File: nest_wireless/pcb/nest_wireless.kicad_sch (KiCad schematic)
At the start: 74 parts, among them J3 Conn_01x04, J4 FFC2B35-12-G_REVA2, SW1 SW_PUSH, SW10 SW_PUSH, SW11 SW_PUSH, SW12 SW_PUSH, SW13 SW_PUSH, SW14 SW_PUSH, SW15 SW_PUSH, SW16 SW_PUSH, SW17 SW_PUSH, SW18 SW_PUSH, SW19 SW_PUSH, SW2 SW_PUSH, SW20 SW_PUSH, SW21 SW_PUSH, SW22 SW_PUSH, SW23 SW_PUSH, SW24 SW_PUSH, SW25 Rotary_Encoder_Switch-Device, SW26 SW_PUSH, SW27 SW_PUSH, SW28 SW_PUSH, SW29 SW_PUSH, SW3 SW_PUSH, SW30 SW_PUSH, SW4 SW_PUSH, SW5 SW_PUSH, SW6 SW_PUSH, SW7 SW_PUSH, SW8 SW_PUSH, SW9 SW_PUSH, U2 kb2040

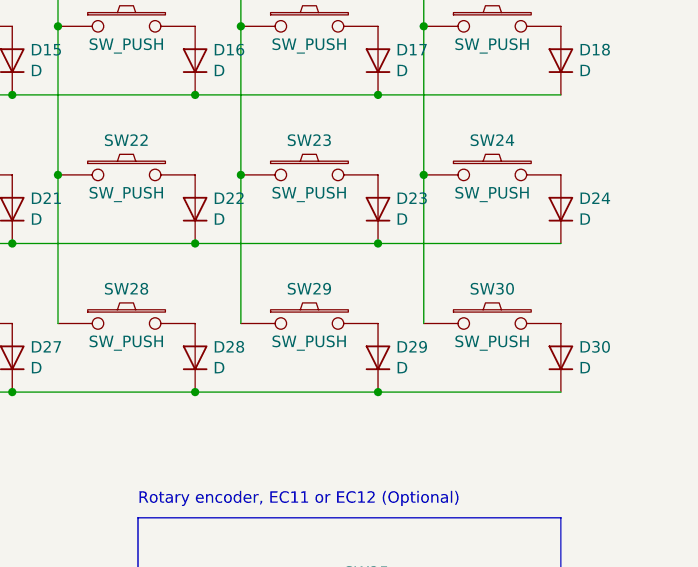
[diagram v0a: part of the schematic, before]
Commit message: Clean up a few design rule violations
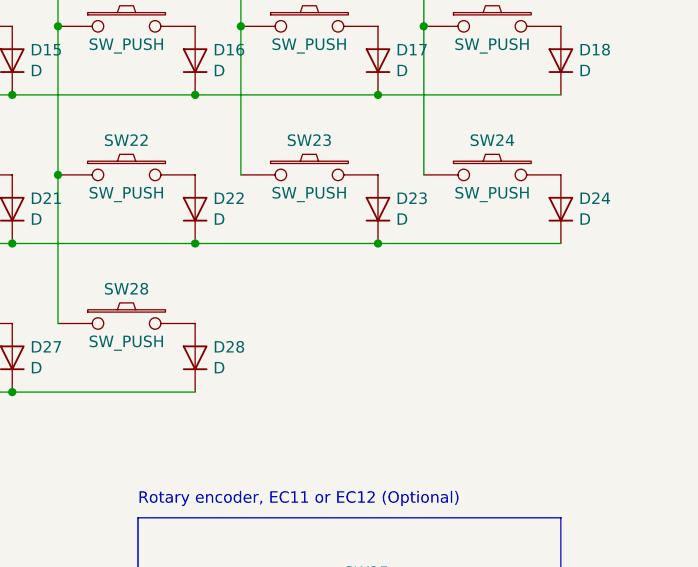
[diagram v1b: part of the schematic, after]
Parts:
- removed D29, D30: D, NestWireless:D_SOD-123_DO-35_Hybrid_DoubleSided_V2, symbol NestWireless:Key_Diode
- removed SW29, SW30: SW_PUSH, NestWireless:Cherry_MX_DS_Hotswap_v3.5.4, symbol NestWireless:SW_PUSH

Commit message: Nest wireless kicad project cleanup
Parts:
- added J1: Conn_01x05, symbol Connector_Generic:Conn_01x05
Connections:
- net ENCA: now also U2.2 (D0); no longer U2.9 (D5)
- net ENCB: now also U2.3 (D1); no longer U2.8 (D4)
- net GND: now also J1.2 (Pin_2)
- net VCC: now also J1.3 (Pin_3)
- net col0: now also U2.19 (A3/29); no longer U2.20 (A2/28)
- net col1: now also U2.20 (A2/28); no longer U2.21 (A1/27)
- net col2: now also U2.21 (A1/27); no longer U2.22 (A0/26)
- net col3: now also U2.22 (A0/26); no longer U2.23 (SCK/18)
- net col5: now also U2.26 (D10); no longer U2.25 (MOSI/19)
- net row0: now also U2.9 (D5); no longer U2.10 (D6)
- net row1: now also U2.10 (D6); no longer U2.11 (D7)
- net row2: now also U2.11 (D7); no longer U2.12 (D8)
- net row3: now also U2.12 (D8); no longer U2.13 (D9)
- net row4: now also U2.13 (D9); no longer U2.26 (D10)
- net RST: now reaches U2.17 (RESET)
- new net CS: J1.1 (Pin_1), U2.8 (D4)
- new net MOSI: J1.5 (Pin_5), U2.25 (MOSI/19)
- new net SCK: J1.4 (Pin_4), U2.23 (SCK/18)
- no-connect marks 6 -> 2
